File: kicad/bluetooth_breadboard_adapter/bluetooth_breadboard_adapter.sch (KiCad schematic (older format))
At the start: 2 parts, among them P1 CONNECTOR, U1 BLK-MD-SPK-B

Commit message: kicad library/module fo rbluetooth module a2dp BLK-MD-SPK-B(-E)
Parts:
- added J1: SCJ368R1NUS0B00G, symbol SCJ368R1NUS0B00G
- added P2: CONNECTOR, ~, symbol CONN_10
- P1: symbol CONN_20 -> CONN_10
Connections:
- net labels added: GND
- wire segments 79 -> 96
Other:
- moved on the sheet: U1

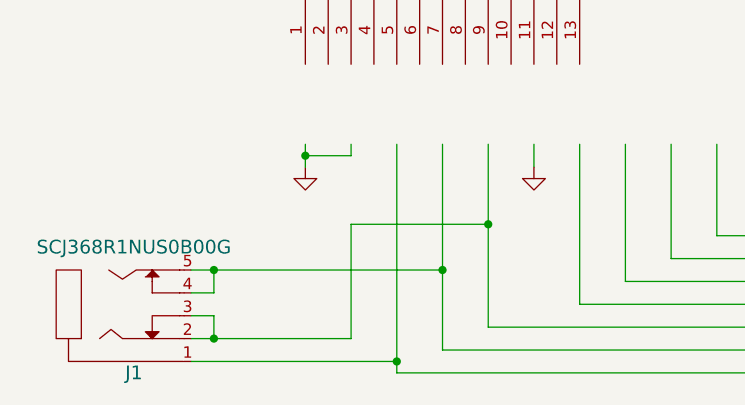
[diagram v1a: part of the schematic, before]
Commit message: 3.5mm jack update to scj-0354-5PU
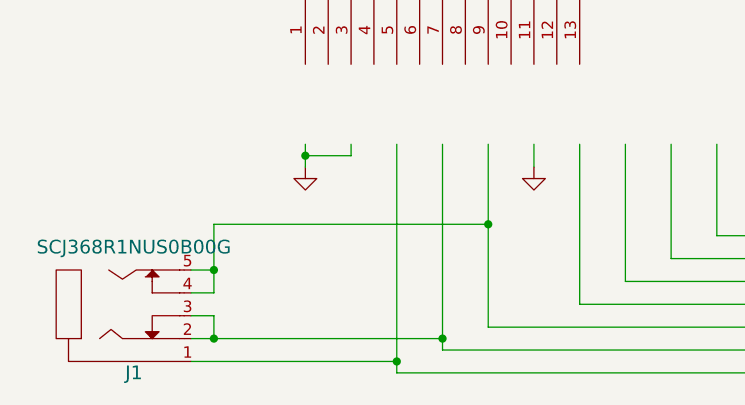
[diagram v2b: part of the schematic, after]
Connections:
- wire segments 96 -> 95
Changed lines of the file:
@@
 LIBS:BLK-MD-SPK-B
 LIBS:bluetooth_breadboard_adapter-cache
-EELAYER 24 0
+EELAYER 25 0
 EELAYER END
 $Descr A4 11693 8268
@@
 Connection ~ 2850 5550
 Wire Wire Line
-	1950 5250 2050 5250
-Wire Wire Line
-	2050 5250 2050 5150
+	2050 5250 1950 5250
+Wire Wire Line
+	2050 4950 2050 5250
 Connection ~ 2050 5150
 Wire Wire Line
@@
 $EndComp
 Wire Wire Line
-	1950 5450 2650 5450
-Wire Wire Line
-	2650 5450 2650 4950
-Wire Wire Line
-	2650 4950 3250 4950
+	2050 4950 3250 4950
 Connection ~ 3250 4950
-Wire Wire Line
-	1950 5150 3050 5150
-Connection ~ 3050 5150
 $Comp
 L GND #PWR?
@@
 	2650 1900 2650 2000
 Connection ~ 2450 1900
+Wire Wire Line
+	2050 5150 1950 5150
+Wire Wire Line
+	1950 5450 3050 5450
+Connection ~ 3050 5450
 $EndSCHEMATC

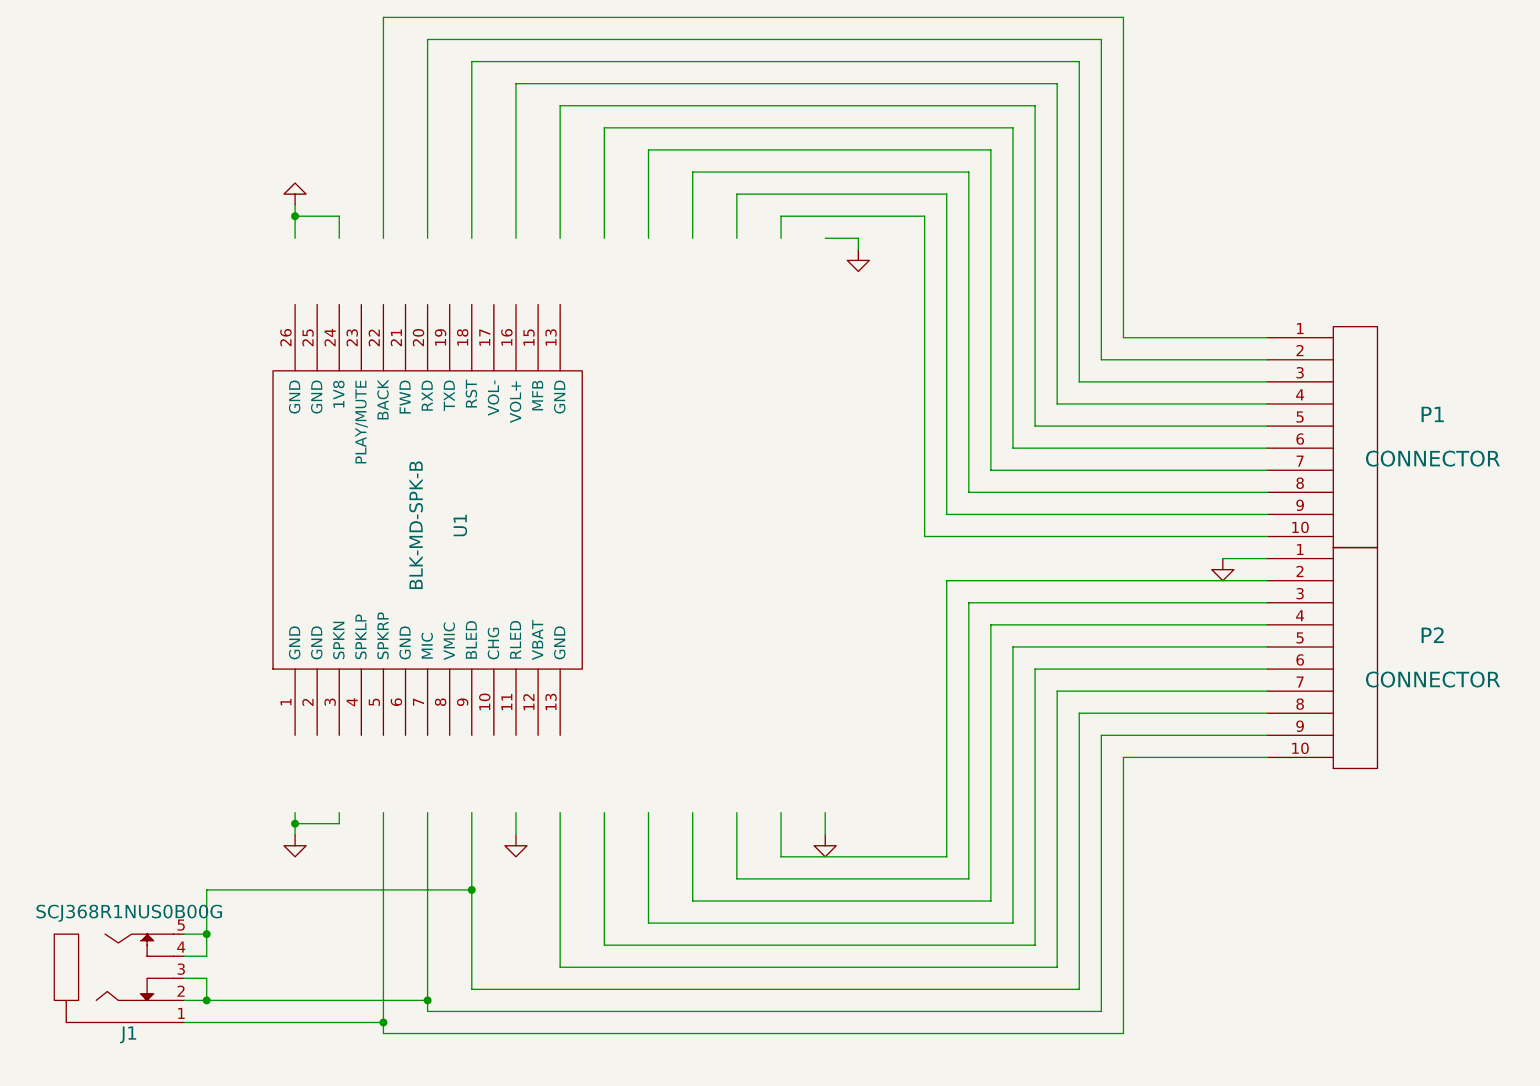
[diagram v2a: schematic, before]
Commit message: schematics with new kicad version
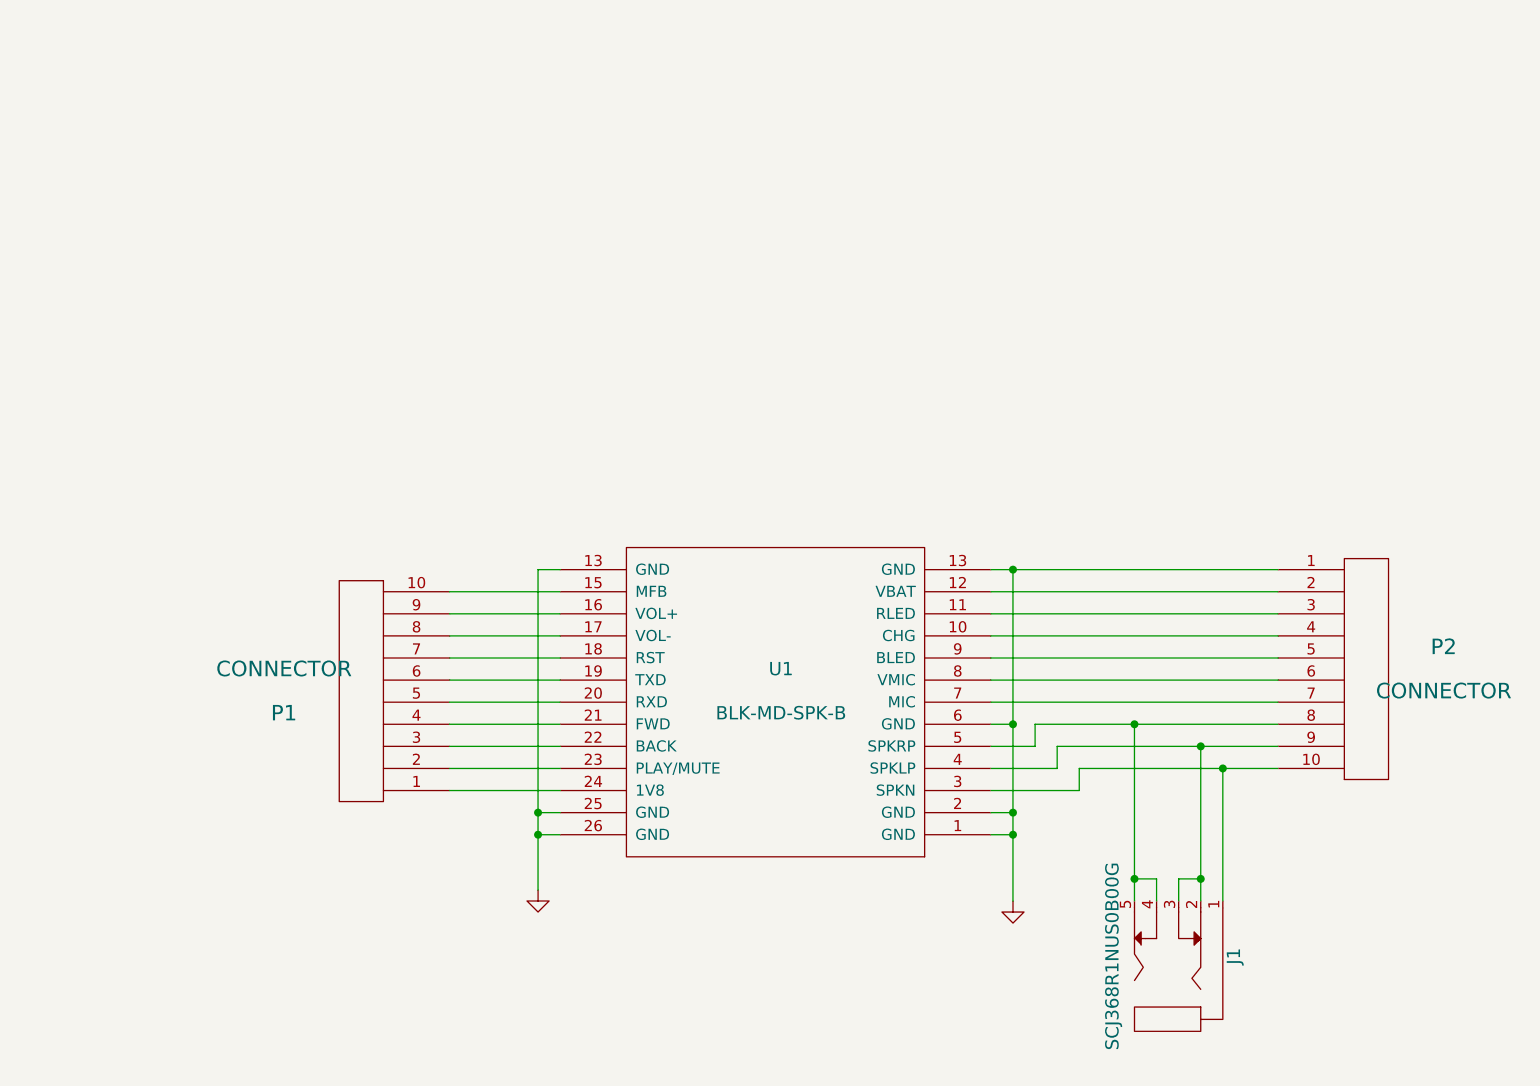
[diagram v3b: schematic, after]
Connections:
- wire segments 95 -> 41
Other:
- moved on the sheet: J1, P1, P2, U1
